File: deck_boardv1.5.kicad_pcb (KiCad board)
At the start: 4 copper layers, 89.2 x 41.3 mm, 56 parts, among them J1 430450800, J2 Conn_01x01_Pin, J3 Conn_01x01_Pin, J4 Conn_01x01_Pin, J5 Conn_01x01_Pin, J6 Conn_01x01_Pin, J7 Conn_01x01_Pin, Q1 MMBT3904, Q2 2N7002, Q3 NMOS, U1 Raspberry Pi Zero 2 W, U2 LT8610AC, U3 DIGI XBee-PRO 900HP RF Module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, U4 ADP7158ARDZ-3.3-R7

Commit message: Adjusted components.
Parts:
- D2, D4, D5, D6: footprint LED_SMD:LED_0603_1608Metric -> LED_THT:LED_D3.0mm
- moved Q1 4.57 mm to (184.6, 91.4), turned to -90 degrees
- moved G*** 3.10 mm to (153.3, 98.3)
- moved R6 3.03 mm to (179.9, 95.4)
- moved R5 2.62 mm to (178.8, 95.4)
- moved R14 2.54 mm to (166.2, 96.2), turned to 0 degrees
- moved D6 2.26 mm to (165.3, 98.9)
- moved D5 2.03 mm to (183.2, 98.9)
- moved D2 1.72 mm to (170.4, 98.9)
- moved R13 1.41 mm to (172.6, 96.2), turned to 180 degrees
- moved D4 1.18 mm to (175.5, 98.9)
- moved U1 0.96 mm to (152.7, 81.8)
- moved R12 0.37 mm to (144.9, 89.1)
- moved R9 0.37 mm to (139.8, 89.1)
- moved R11 0.37 mm to (144.9, 90.3)
- moved R10 0.37 mm to (139.9, 90.3)
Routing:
- net Net-(Q1-B): track 2.75 -> 10.3 mm
- net Net-(D5-K): track 11.8 -> 7.12 mm
- net GPIO15: track 56.7 -> 60.3 mm
- net Net-(D4-A): track 1.27 -> 3.49 mm
- net Net-(D6-A): track 1.26 -> 3.20 mm
- net Net-(D2-A): track 1.25 -> 2.62 mm
- net Net-(D5-A): track 2.12 -> 3.46 mm
- net XBee_ASSOC: track 35.8 -> 34.7 mm
- net ENABLE: track 102.0 -> 100.9 mm
- net GPIO24: track 51.9 -> 51.0 mm
- net Net-(U1-GPIO22/GPIO_GEN3): track 4.07 -> 3.39 mm
- net Net-(U1-GPIO17/GPIO_GEN0): track 4.06 -> 3.38 mm
- net GND: vias 4 -> 1

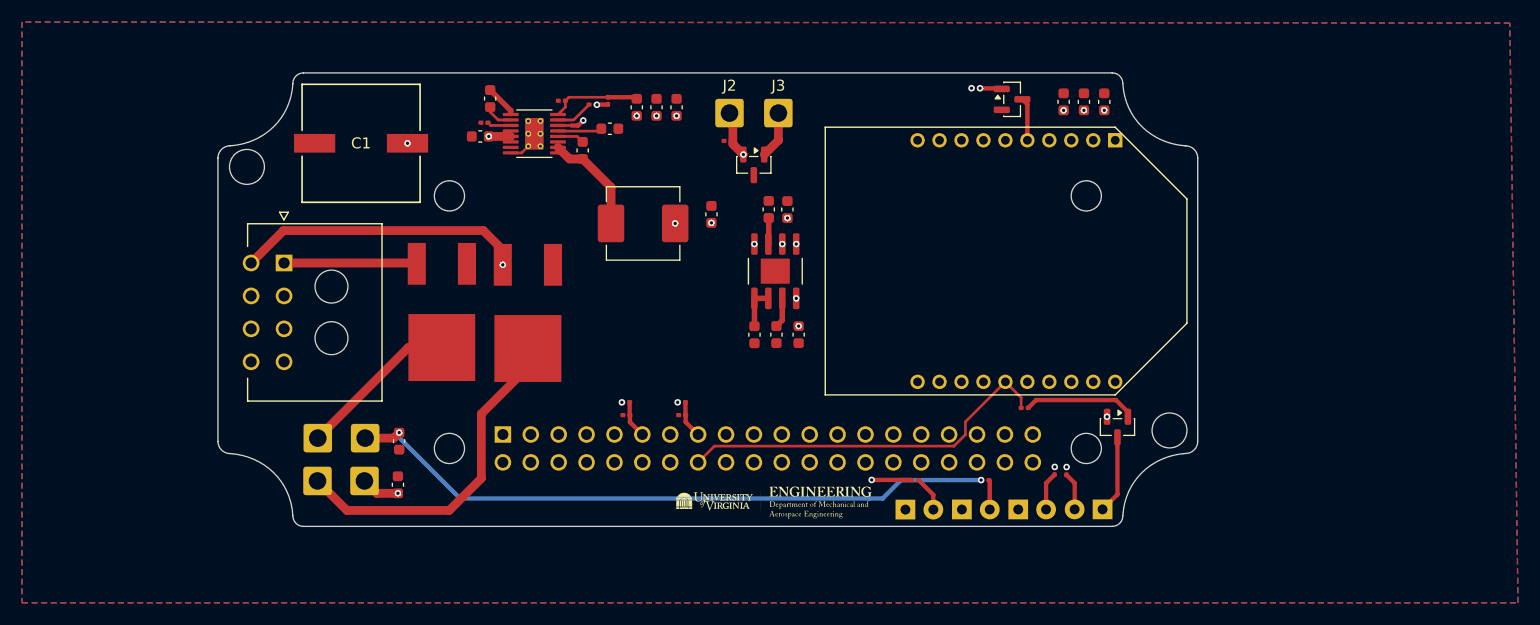
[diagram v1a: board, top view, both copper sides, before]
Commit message: Added labels to silkscreen.
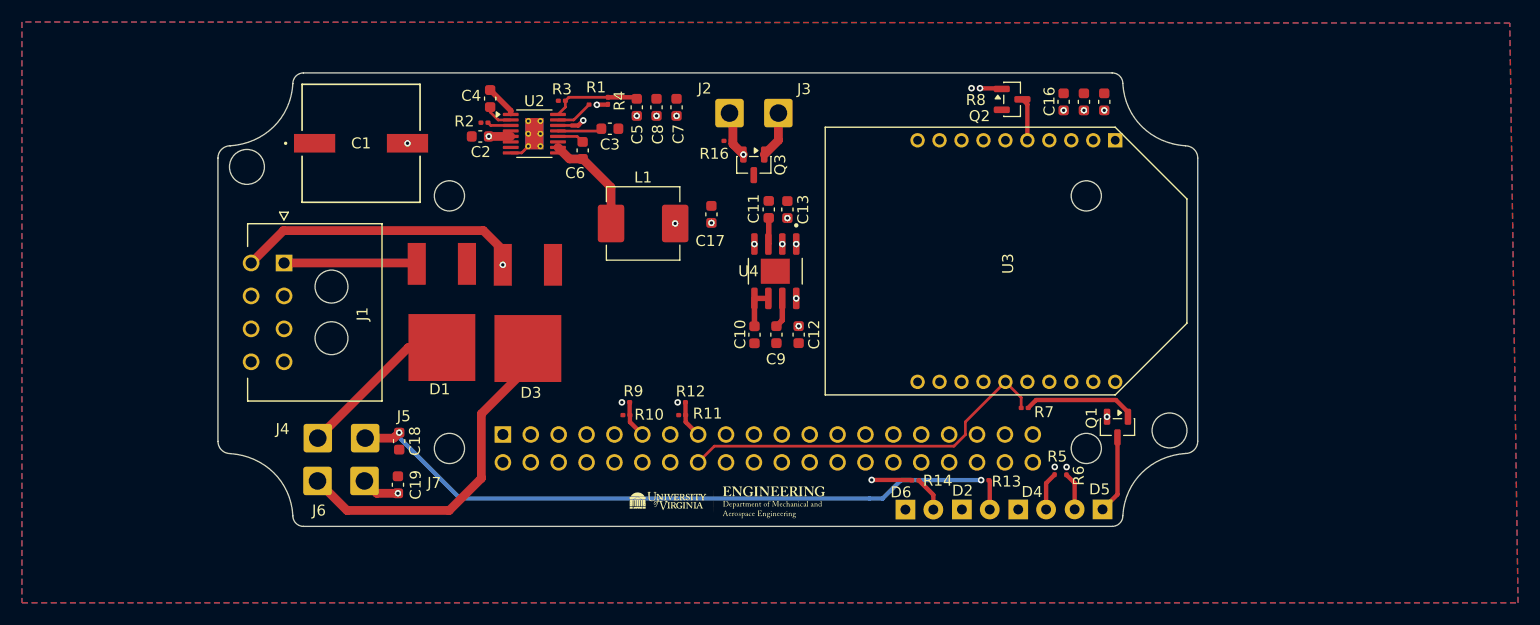
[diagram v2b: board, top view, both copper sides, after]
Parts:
- moved G*** 4.24 mm to (149.1, 98.2)

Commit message: Made adjustments.
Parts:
- moved D4 0.08 mm to (175.6, 98.8)
- moved D2 0.08 mm to (170.4, 98.8)
- moved D5 0.08 mm to (183.2, 98.8)
- moved D6 0.08 mm to (165.3, 98.8)
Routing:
- net 5V_Pi: track 3.58 -> 71.2 mm, vias 10 -> 6
- net 3V3: track 0.00 -> 15.0 mm, vias 9 -> 4
- net 28V_POST-INHIB: track 97.9 -> 101.9 mm, vias 4 -> 3
- net GND: track 4.77 -> 6.62 mm
- net TE_2: track 47.3 -> 48.4 mm
- net GPIO15: track 60.3 -> 61.0 mm, vias 0 -> 1
- net GPIO24: track 51.0 -> 51.3 mm, vias 1 -> 2
- net GPIO14: vias 0 -> 1
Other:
- board size 89.2 x 41.3 mm -> 91 x 42.1 mm

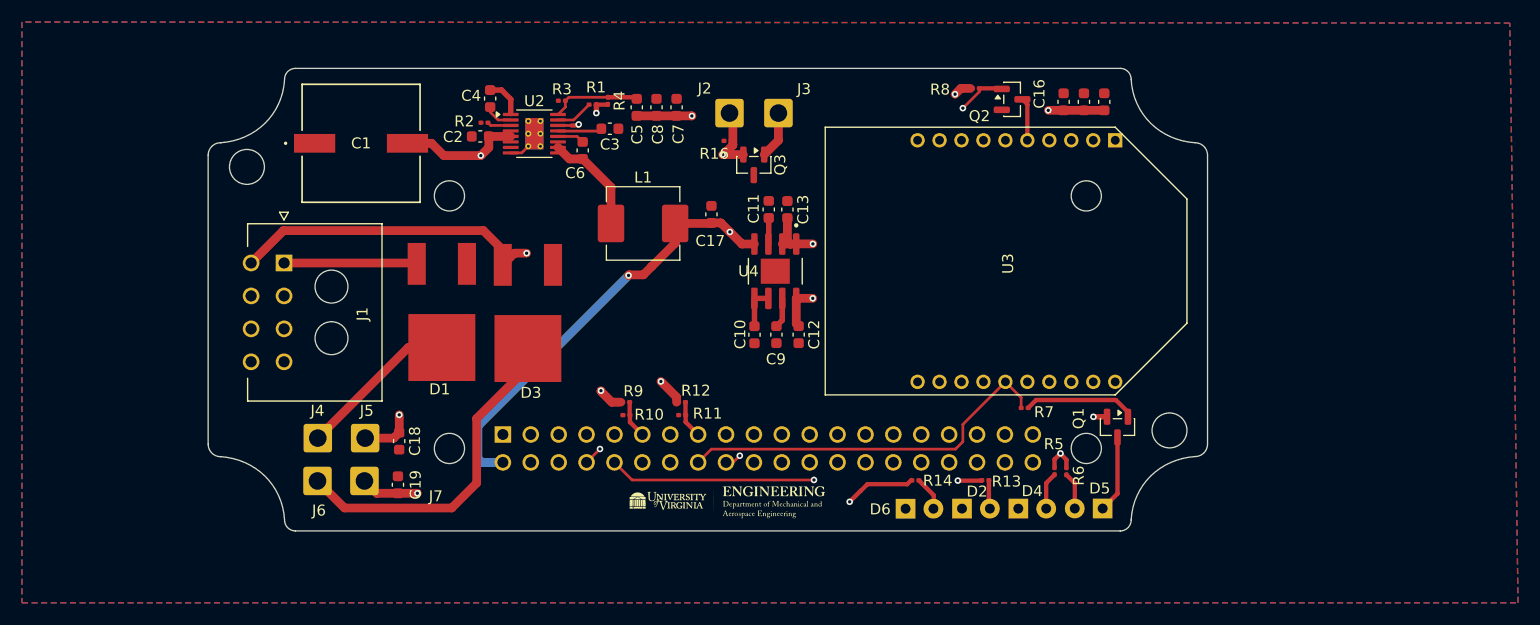
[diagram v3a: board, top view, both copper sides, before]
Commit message: Fixed footprint sizes.
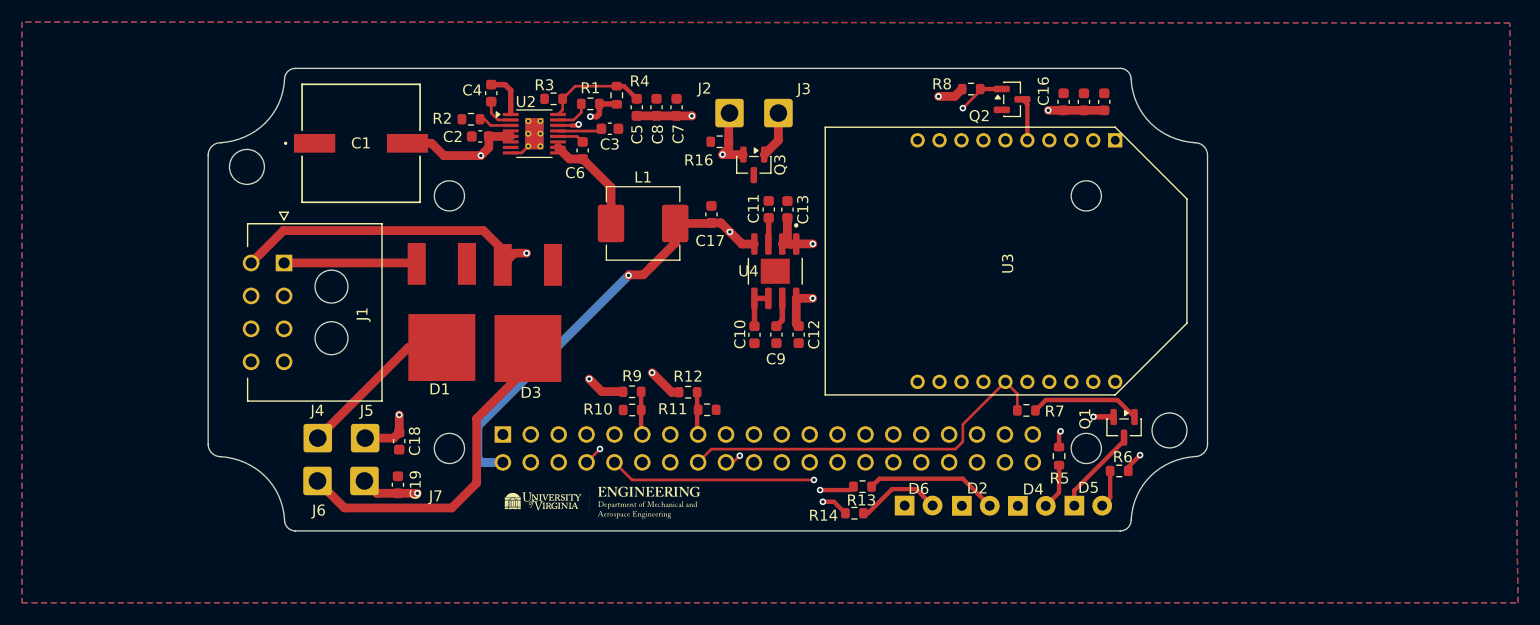
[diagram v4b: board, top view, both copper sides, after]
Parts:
- R1, R10, R11, R12, R13, R14, R16, R2, R3, R4, R5, R6, R7, R8, R9: footprint Resistor_SMD:R_0201_0603Metric -> Resistor_SMD:R_0603_1608Metric
- moved G*** 11.4 mm to (137.7, 98.3)
- moved R13 11.2 mm to (161.4, 96.8)
- moved R14 6.30 mm to (160.6, 99.2)
- moved R6 4.81 mm to (184.7, 95.4), turned to 0 degrees
- moved D5 2.59 mm to (180.7, 98.5), turned to 0 degrees
- moved R11 2.33 mm to (147.2, 89.8), turned to 0 degrees
- moved R5 1.43 mm to (179.3, 94.0)
- moved R2 1.26 mm to (125.7, 63.4)
- moved R9 1.09 mm to (140.4, 88.2)
- moved R12 1.07 mm to (145.5, 88.2)
- moved R4 0.95 mm to (139.0, 61.2)
- moved R3 0.78 mm to (133.2, 61.5)
- moved R16 0.71 mm to (148.4, 65.4)
- moved R10 0.70 mm to (140.4, 89.8)
- moved Q1 0.60 mm to (185.2, 91.4)
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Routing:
- net 28V_POST-INHIB: track 101.9 -> 90.0 mm
- net Net-(D2-A): track 2.62 -> 12.1 mm
- net ENABLE: track 100.8 -> 94.6 mm
- net Net-(D6-A): track 2.92 -> 7.82 mm
- net GND: track 6.62 -> 8.41 mm
- net 5V_Pi: track 71.2 -> 72.8 mm
- net 3V3: track 15.0 -> 16.2 mm, vias 4 -> 5
- net Net-(U2-FB): track 8.22 -> 9.30 mm
- net Net-(D5-K): track 7.04 -> 8.07 mm
- net Net-(U2-RT): track 2.18 -> 3.03 mm
- net Net-(D4-A): track 3.40 -> 4.21 mm
- net Net-(U1-GPIO17/GPIO_GEN0): track 3.38 -> 3.94 mm

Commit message: Fixed footprints.
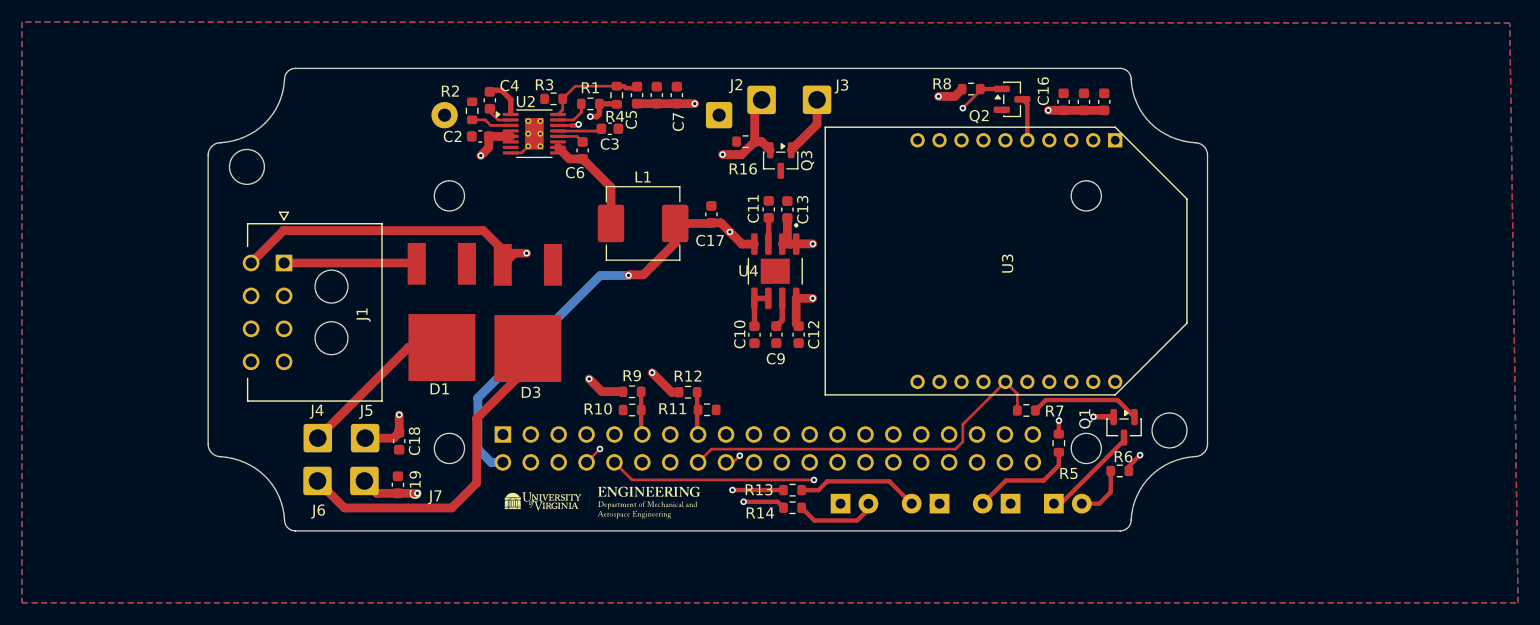
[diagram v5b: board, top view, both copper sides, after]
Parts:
- C1: footprint APZ1012470M100R:CAP_APZ_1012_KAV -> Capacitor_THT:CP_Axial_L18.0mm_D8.0mm_P25.00mm_Horizontal; moved to B.Cu
- D2, D4, D5, D6: footprint LED_THT:LED_D3.0mm -> LED_THT:LED_D5.0mm
- moved C1 32.7 mm to (148.3, 63.0), turned to 180 degrees
- moved R13 6.38 mm to (155.0, 97.1)
- moved D6 5.84 mm to (159.4, 98.4)
- moved R14 5.66 mm to (155.0, 98.7)
- moved J3 3.72 mm to (157.2, 61.6)
- moved J2 3.16 mm to (152.2, 61.6)
- moved Q3 2.48 mm to (153.9, 67.1)
- moved R16 2.36 mm to (150.7, 65.4)
- moved D2 2.04 mm to (168.4, 98.4), turned to 180 degrees
- moved D5 1.87 mm to (178.8, 98.4)
- moved R5 1.18 mm to (179.2, 92.9)
- moved C8 1.11 mm to (142.6, 61.2)
- moved C5 1.11 mm to (140.8, 61.2)
- moved C7 1.11 mm to (144.5, 61.2)
- moved R2 0.77 mm to (125.8, 62.6), turned to 90 degrees
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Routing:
- net 5V_Pi: track 72.8 -> 55.9 mm
- net 28V_POST-INHIB: track 90.0 -> 80.7 mm
- net Net-(D4-A): track 4.21 -> 9.57 mm
- net ENABLE: track 94.6 -> 91.6 mm
- net Net-(D5-A): track 3.46 -> 5.00 mm
- net Net-(D5-K): track 8.07 -> 9.34 mm
- net Net-(J3-Pin_1): track 4.31 -> 5.57 mm
- net Net-(D2-A): track 12.1 -> 11.2 mm
- net Net-(U2-RT): track 3.03 -> 3.77 mm
- net Net-(U2-TR/SS): track 3.07 -> 2.48 mm

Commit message: Fixed general issues with footprints.
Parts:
- L1: footprint Inductor_SMD:L_Vishay_IHLP-2525 -> Library:0630CDMCCDS-100MC
- moved J1 8.71 mm to (111.4, 84.7), turned to -90 degrees
- moved D3 7.13 mm to (125.7, 76.8), turned to -90 degrees
- moved D1 6.44 mm to (128.8, 84.5), turned to 90 degrees
- moved R2 0.19 mm to (126.0, 62.6)
- moved C4 0.15 mm to (127.6, 61.6)
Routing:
- net Net-(J4-Pin_1): track 14.7 -> 22.9 mm
- net TE_2: track 48.0 -> 43.8 mm, vias 2 -> 0
- net TE_1: track 34.2 -> 32.1 mm
- net 28V: track 12.1 -> 13.2 mm
- net 5V_Pi: track 55.9 -> 56.4 mm
- net Net-(C6-Pad1): track 9.63 -> 10.1 mm
